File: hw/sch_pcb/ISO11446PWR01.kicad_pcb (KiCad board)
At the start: 2 copper layers, 40.1 x 40.1 mm, 17 parts, among them J1 HEADER_2x04_PARALLEL, J2 HEADER_2x04_PARALLEL, J3 HEADER_2x04_PARALLEL, J4 Conn_01x01_Female, J5 Conn_01x01_Female, J6 Conn_01x01_Female, J7 Conn_01x01_Female, J8 Umin ... Umax, M1 HOLE M3, M2 HOLE M3, M3 HOLE, M4 HOLE

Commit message: An initial test implementation. Both Schema and PCB needs check.
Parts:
- added D1: LED, Mlab_D:LED_1206, B.Cu at (169.1, 90.3)
- added D2: LED, Mlab_D:LED_1206, B.Cu at (138.6, 140.2)
- added D3: LED, Mlab_D:LED_1206, B.Cu at (129.3, 86.8)
- added D4: LED, Mlab_D:LED_1206, B.Cu at (129.2, 96.9)
- added D5: LED, Mlab_D:LED_1206, B.Cu at (129.3, 71.4)
- added D6: LED, Mlab_D:LED_1206, B.Cu at (129.3, 76.6)
- added D7: LED, Mlab_D:LED_1206, B.Cu at (129.3, 91.6)
- added D8: LED, Mlab_D:LED_1206, B.Cu at (129.2, 102.0)
- added D9: LED, Mlab_D:LED_1206, B.Cu at (129.3, 107.0)
- added F1: Polyfuse, Mlab_F:1812, B.Cu at (159.9, 132.2)
- added F4: Polyfuse, Mlab_F:1812, B.Cu at (146.5, 144.4)
- added J10: 10 - Spínané 12V +, Mlab_CON:WAGO256, F.Cu at (120.5, 116.9)
- added J11: 11 - Spínané 12V -, Mlab_CON:WAGO256, F.Cu at (120.5, 122.0)
- added J12: 12 - Not used, Mlab_CON:WAGO256, F.Cu at (120.5, 127.1)
- added J13: 13 - Trvalé 12V -, Mlab_CON:WAGO256, F.Cu at (120.5, 132.1)
- added J15: 13 - Trvalé 12V +, Mlab_CON:WAGO256, F.Cu at (178.7, 85.7)
- added J16: 13 - Trvalé 12V -, Mlab_CON:WAGO256, F.Cu at (178.7, 90.8)
- added J17: 13 - Spínané 12V +, Mlab_CON:WAGO256, F.Cu at (128.2, 144.4)
- added J18: 13 - Spínané 12V -, Mlab_CON:WAGO256, F.Cu at (128.2, 139.2)
- added J21: Signal Světel, Mlab_Pin_Headers:Straight_2x07, F.Cu at (174.2, 69.8)
- added J5: 5 - Obrsové P, Mlab_CON:WAGO256, F.Cu at (120.5, 91.5)
- added J6: 6 - Brzdové, Mlab_CON:WAGO256, F.Cu at (120.5, 96.6)
- added J7: 7 - Obrysové L, Mlab_CON:WAGO256, F.Cu at (120.5, 101.7)
- added J8: 8 - Couvací, Mlab_CON:WAGO256, F.Cu at (120.5, 106.7)
- added J9: 9 - Trvalé 12V +, Mlab_CON:WAGO256, F.Cu at (120.5, 111.8)
- added R1: 800, Mlab_R:SMD-0805, B.Cu at (169.1, 85.3)
- added R10: 240, Mlab_R:SMD-0805, B.Cu at (142.6, 104.9)
- added R11: 240, Mlab_R:SMD-0805, B.Cu at (144.4, 71.7)
- added R12: 800, Mlab_R:SMD-0805, B.Cu at (138.6, 144.3)
- added R13: 240, Mlab_R:SMD-0805, B.Cu at (152.6, 84.4)
- added R14: 240, Mlab_R:SMD-0805, B.Cu at (154.8, 105.4)
- added R15: 240, Mlab_R:SMD-0805, B.Cu at (156.3, 68.2)
- added R16: 240, Mlab_R:SMD-0805, B.Cu at (144.4, 76.2)
- added R17: 240, Mlab_R:SMD-0805, B.Cu at (140.4, 94.8)
- added R18: 240, Mlab_R:SMD-0805, B.Cu at (146.1, 115.7)
- added R19: 240, Mlab_R:SMD-0805, B.Cu at (156.6, 76.2)
- added R2: 36, Mlab_R:R_Axial_Power_L22.0mm_W9.5mm_P30.48mm, F.Cu at (134.0, 67.7)
- added R20: 240, Mlab_R:SMD-0805, B.Cu at (152.7, 94.5)
- added R21: 240, Mlab_R:SMD-0805, B.Cu at (158.3, 115.5)
- added R22: 240, Mlab_R:SMD-0805, B.Cu at (146.0, 126.3)
- added R23: 240, Mlab_R:SMD-0805, B.Cu at (158.1, 126.2)
- added R3: 36, Mlab_R:R_Axial_Power_L22.0mm_W9.5mm_P30.48mm, F.Cu at (134.0, 78.1)
- added R4: 36, Mlab_R:R_Axial_Power_L22.0mm_W9.5mm_P30.48mm, F.Cu at (134.1, 89.8)
- added R5: 36, Mlab_R:R_Axial_Power_L22.0mm_W9.5mm_P30.48mm, F.Cu at (136.7, 100.0)
- added R6: 36, Mlab_R:R_Axial_Power_L22.0mm_W9.5mm_P30.48mm, F.Cu at (140.0, 110.3)
- added R7: 36, Mlab_R:R_Axial_Power_L22.0mm_W9.5mm_P30.48mm, F.Cu at (140.1, 121.2)
- added R8: 36, Mlab_R:R_Axial_Power_L22.0mm_W9.5mm_P30.48mm, F.Cu at (140.1, 131.3)
- added R9: 240, Mlab_R:SMD-0805, B.Cu at (140.3, 84.7)
- added U1: LTV-357T, Package_SO:SO-4_4.4x3.6mm_P2.54mm, B.Cu at (146.1, 84.3)
- added U2: LTV-357T, Package_SO:SO-4_4.4x3.6mm_P2.54mm, B.Cu at (148.4, 105.4)
- added U3: LTV-357T, Package_SO:SO-4_4.4x3.6mm_P2.54mm, B.Cu at (150.0, 68.2)
- added U4: LTV-357T, Package_SO:SO-4_4.4x3.6mm_P2.54mm, B.Cu at (150.3, 76.2)
- added U5: LTV-357T, Package_SO:SO-4_4.4x3.6mm_P2.54mm, B.Cu at (146.2, 94.6)
- added U6: LTV-357T, Package_SO:SO-4_4.4x3.6mm_P2.54mm, B.Cu at (151.9, 115.5)
- added U7: LTV-357T, Package_SO:SO-4_4.4x3.6mm_P2.54mm, B.Cu at (151.8, 126.2)
- C1: footprint Capacitor_SMD:C_0805_2012Metric -> Mlab_C:SMD-0805
- F2: renamed from F1; footprint Fuse:Fuse_Bourns_MF-RG400 -> Fuse:Fuseholder_Keystone_3555-2
- F3: renamed from F2; footprint Fuse:Fuse_Bourns_MF-RG400 -> Mlab_F:1812; moved to B.Cu
- J1: renamed from J4; value Conn_01x01_Female -> 1 - Směrové L
- J14: renamed from J3; value HEADER_2x04_PARALLEL -> Trvalé 12V
- J19: renamed from J1; value HEADER_2x04_PARALLEL -> Ventilator 12V
- J2: renamed from J5; value Conn_01x01_Female -> 2 - Zadní mlhové
- J20: renamed from J2; value HEADER_2x04_PARALLEL -> Spinane 12V
- J22: renamed from J8; value Umin ... Umax -> Umin ... 5V
- J3: renamed from J6; value Conn_01x01_Female -> 3 - Kostra světla
- J4: renamed from J7; value Conn_01x01_Female -> 4 - Směrové P
- moved J20 121.1 mm to (147.5, 139.7), turned to -90 degrees
- moved J19 118.2 mm to (160.5, 139.7), turned to -90 degrees
- moved J2 110.0 mm to (120.5, 76.3), turned to 180 degrees
- moved J1 104.7 mm to (120.5, 71.2), turned to 180 degrees
- moved J3 102.7 mm to (120.5, 81.3), turned to 180 degrees
- moved J4 100.9 mm to (120.5, 86.4), turned to 180 degrees
- moved J14 98.7 mm to (173.4, 139.8), turned to 90 degrees
- moved M2 74.1 mm to (183.8, 64.1)
- moved F3 73.8 mm to (159.5, 144.5)
- moved M4 53.5 mm to (183.8, 145.4)
- moved F2 50.7 mm to (176.7, 129.4), turned to 90 degrees
- moved J22 36.8 mm to (124.1, 64.5), turned to -90 degrees
- moved C1 34.9 mm to (140.6, 72.1), turned to 0 degrees
- moved M1 34.2 mm to (112.7, 64.1)
- moved M3 33.6 mm to (112.7, 145.4)
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- renumbered D1 to D10
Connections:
- F2 pad 1: Net-(F1-Pad1) -> U12+
- F2 pad 2: Net-(F1-Pad2) -> Net-(F2-Pad2)
- F3 pad 1: Net-(F2-Pad1) -> S12+
- F3 pad 2: Net-(F2-Pad2) -> Net-(F3-Pad2)
- J1 pad 1: Net-(F1-Pad2) -> L1
- J14 pad 1: unconnected-(J3-Pad1) -> U12-
- J14 pad 2: unconnected-(J3-Pad1) -> U12-
- J14 pad 3: unconnected-(J3-Pad3) -> Net-(F1-Pad2)
- J14 pad 4: unconnected-(J3-Pad3) -> Net-(F1-Pad2)
- J14 pad 5: unconnected-(J3-Pad5) -> Net-(F1-Pad2)
- J14 pad 6: unconnected-(J3-Pad5) -> Net-(F1-Pad2)
- J14 pad 7: Net-(J1-Pad1) -> U12-
- J14 pad 8: Net-(J1-Pad1) -> U12-
- J19 pad 1: Net-(J1-Pad1) -> S12-
- J19 pad 2: Net-(J1-Pad1) -> S12-
- J19 pad 3: Net-(J1-Pad3) -> Net-(F3-Pad2)
- J19 pad 4: Net-(J1-Pad3) -> Net-(F3-Pad2)
- J19 pad 5: Net-(F2-Pad1) -> Net-(F3-Pad2)
- J19 pad 6: Net-(F2-Pad1) -> Net-(F3-Pad2)
- J19 pad 7: Net-(F1-Pad1) -> S12-
- J19 pad 8: Net-(F1-Pad1) -> S12-
- J2 pad 1: Net-(F2-Pad2) -> L2
- J20 pad 1: unconnected-(J2-Pad1) -> S12-
- J20 pad 2: unconnected-(J2-Pad1) -> S12-
- J20 pad 3: unconnected-(J2-Pad3) -> Net-(F4-Pad2)
- J20 pad 4: unconnected-(J2-Pad3) -> Net-(F4-Pad2)
- J20 pad 5: Net-(F1-Pad1) -> Net-(F4-Pad2)
- J20 pad 6: Net-(F1-Pad1) -> Net-(F4-Pad2)
- J20 pad 7: Net-(F1-Pad1) -> S12-
- J20 pad 8: Net-(F1-Pad1) -> S12-
- J3 pad 1: Net-(J1-Pad3) -> L_GND
- J4 pad 1: Net-(J1-Pad1) -> L4
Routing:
- net Net-(M1-Pad1): track 0.00 -> 235.8 mm
- net L_GND: track 0.00 -> 166.0 mm
- net +5V: track 0.00 -> 155.1 mm
- net GND: track 0.00 -> 143.4 mm
- net U12-: track 0.00 -> 135.0 mm
- net U12+: track 0.00 -> 92.7 mm
- net L8S: track 0.00 -> 90.2 mm
- net S12-: track 0.00 -> 89.9 mm
- net S12+: track 0.00 -> 83.6 mm
- net L7S: track 0.00 -> 78.2 mm
- net L6S: track 0.00 -> 68.3 mm
- net L5S: track 0.00 -> 57.1 mm
- net Net-(F2-Pad2): track 0.00 -> 45.8 mm
- net L4S: track 0.00 -> 45.2 mm
- net L8: track 0.00 -> 40.4 mm
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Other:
- board size 40.1 x 40.1 mm -> 80.8 x 90.9 mm

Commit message: slove some warnings.
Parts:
- moved D1 0.61 mm to (168.5, 90.1)
- moved J15 0.61 mm to (178.1, 85.5)
- moved J16 0.61 mm to (178.1, 90.6)
- moved R1 0.61 mm to (168.5, 85.1)
- moved D4 0.40 mm to (129.6, 96.7)
- moved D8 0.38 mm to (129.6, 102.0)
- moved D7 0.24 mm to (129.6, 91.5)
- moved D3 0.24 mm to (129.6, 86.7)
- moved D5 0.24 mm to (129.6, 71.5)
- moved D6 0.24 mm to (129.6, 76.6)
- moved R12 0.19 mm to (138.6, 144.5)
- moved D9 0.13 mm to (129.4, 107.0)
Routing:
- net L_GND: track 166.0 -> 208.7 mm
- net Net-(M1-Pad1): track 235.8 -> 230.8 mm
- net Net-(U6-Pad1): track 0.00 -> 2.72 mm
- net GND: track 143.4 -> 140.9 mm
- net S12-: track 89.9 -> 88.2 mm
- net L1: track 20.2 -> 18.6 mm
- net Net-(F1-Pad2): track 22.3 -> 21.4 mm
- net Net-(F4-Pad2): track 12.0 -> 11.2 mm
- net +5V: track 155.1 -> 154.5 mm
- net U12-: track 135.0 -> 134.4 mm
- net Net-(F2-Pad2): track 45.8 -> 46.4 mm

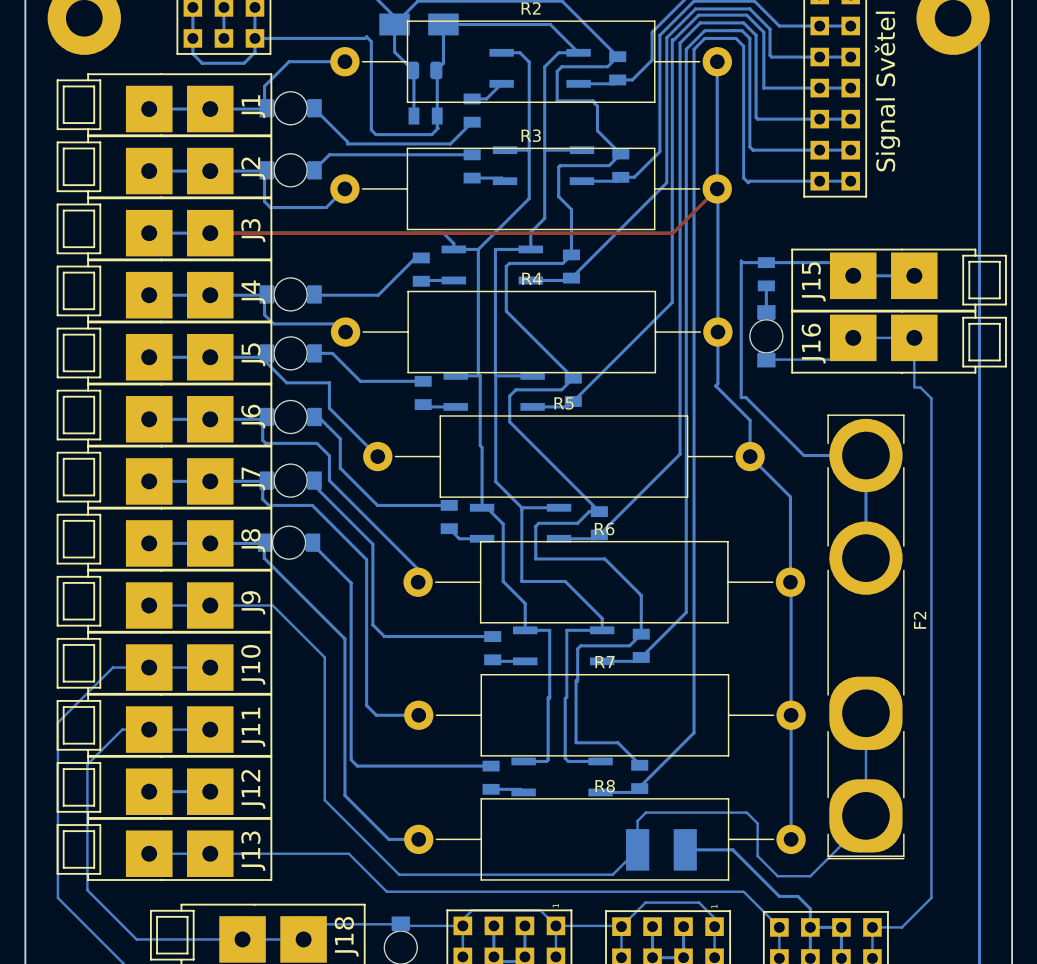
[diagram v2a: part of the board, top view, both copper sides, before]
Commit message: Improve layout and connector orientation.
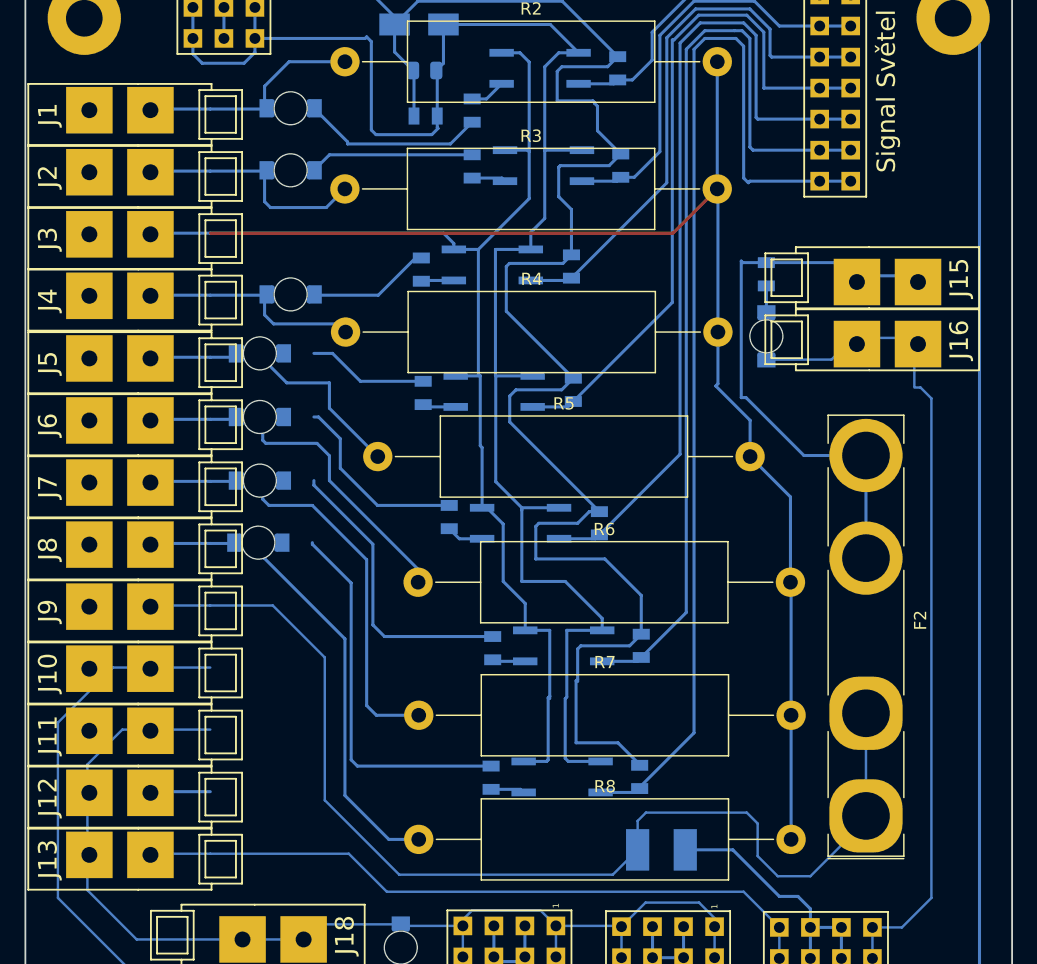
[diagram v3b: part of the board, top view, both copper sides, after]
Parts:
- moved J1 5.04 mm to (115.6, 72.0), turned to 0 degrees
- moved J10 5.04 mm to (115.6, 117.7), turned to 0 degrees
- moved J11 5.04 mm to (115.6, 122.8), turned to 0 degrees
- moved J12 5.04 mm to (115.6, 127.9), turned to 0 degrees
- moved J13 5.04 mm to (115.6, 132.9), turned to 0 degrees
- moved J2 5.04 mm to (115.6, 77.1), turned to 0 degrees
- moved J3 5.04 mm to (115.6, 82.1), turned to 0 degrees
- moved J5 5.04 mm to (115.6, 92.3), turned to 0 degrees
- moved J6 5.04 mm to (115.6, 97.4), turned to 0 degrees
- moved J7 5.04 mm to (115.6, 102.5), turned to 0 degrees
- moved J8 5.04 mm to (115.6, 107.5), turned to 0 degrees
- moved J9 5.04 mm to (115.6, 112.6), turned to 0 degrees
- moved J4 5.03 mm to (115.6, 87.2), turned to 0 degrees
- moved D4 2.52 mm to (127.1, 96.7)
- moved D7 2.52 mm to (127.1, 91.5)
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
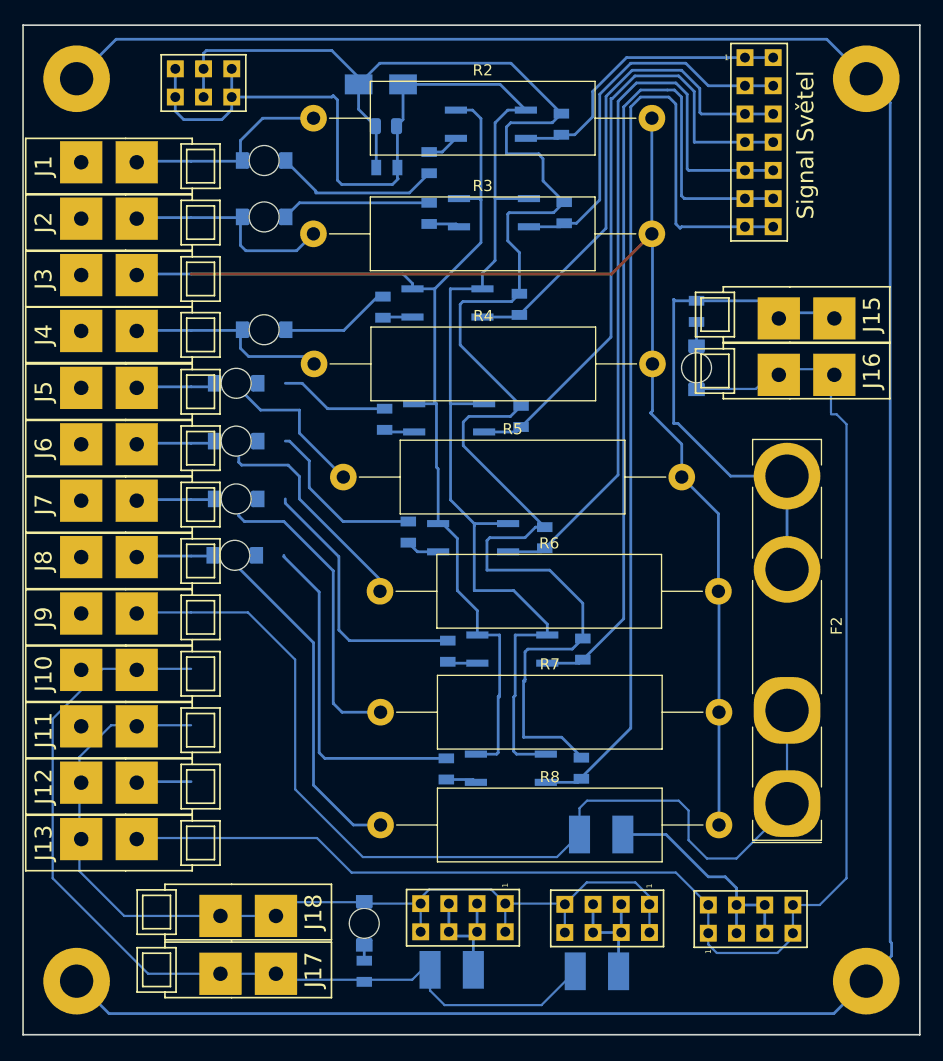
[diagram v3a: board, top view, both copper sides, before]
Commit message: Significant schematic and layout improvement. Fixed fuse footprint Fixed schematics   * Spliting to multiple sheets   * Texts translated from czech to english
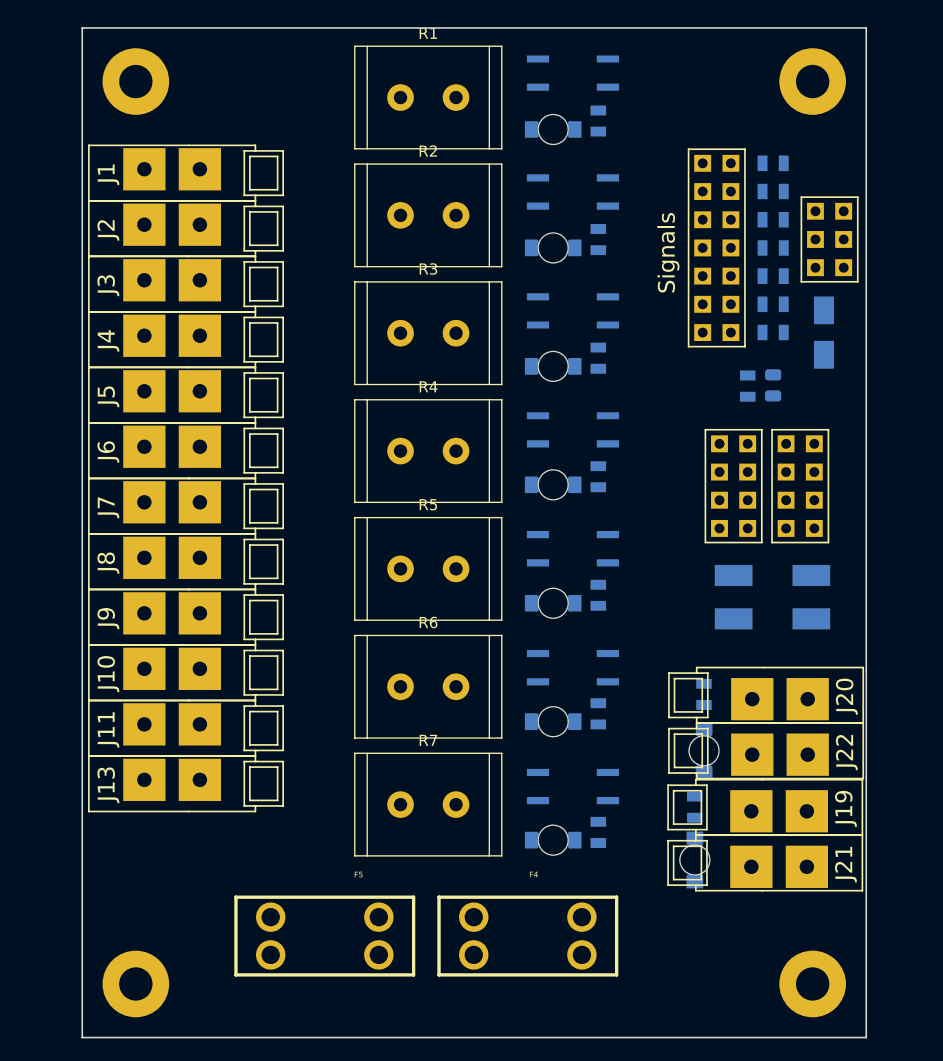
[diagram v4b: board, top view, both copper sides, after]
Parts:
- removed F2: Fuse, Fuse:Fuseholder_Keystone_3555-2
- removed J12: 12 - Not used, Mlab_CON:WAGO256
- removed J17: 13 - Spínané 12V +, Mlab_CON:WAGO256
- added F5: 16A, Mlab_CON:Fuse-Keystone-3557-2, F.Cu at (135.0, 141.3)
- D1: value LED -> BZV55C-5,6V; footprint Mlab_D:LED_1206 -> Diode_SMD:D_SMA
- D10: value BZV55C-5,6V -> LED; footprint Diode_SMD:D_SMA -> Mlab_D:LED_1206
- F1, F3: value Polyfuse -> SD110-16
- F4: value Polyfuse -> 16A; footprint Mlab_F:1812 -> Mlab_CON:Fuse-Keystone-3557-2; moved to F.Cu
- J1: value 1 - Směrové L -> WAGO 256-401
- J10: value 10 - Spínané 12V + -> WAGO 256-401
- J11: value 11 - Spínané 12V - -> WAGO 256-401
- J13: value 13 - Trvalé 12V - -> WAGO 256-401
- J14: value Trvalé 12V -> 3.3-5V; footprint Mlab_Pin_Headers:Straight_2x04 -> Mlab_Pin_Headers:Straight_2x03
- J15: value 13 - Trvalé 12V + -> Signals; footprint Mlab_CON:WAGO256 -> Mlab_Pin_Headers:Straight_2x07
- J16: value 13 - Trvalé 12V - -> 2x4; footprint Mlab_CON:WAGO256 -> Mlab_Pin_Headers:Straight_2x04
- J18: value 13 - Spínané 12V - -> 2x4; footprint Mlab_CON:WAGO256 -> Mlab_Pin_Headers:Straight_2x04
- J19: value Ventilator 12V -> WAGO 256-401; footprint Mlab_Pin_Headers:Straight_2x04 -> Mlab_CON:WAGO256
- J2: value 2 - Zadní mlhové -> WAGO 256-401
- J20: value Spinane 12V -> WAGO 256-401; footprint Mlab_Pin_Headers:Straight_2x04 -> Mlab_CON:WAGO256
- J21: value Signal Světel -> WAGO 256-401; footprint Mlab_Pin_Headers:Straight_2x07 -> Mlab_CON:WAGO256
- J22: value Umin ... 5V -> WAGO 256-401; footprint Mlab_Pin_Headers:Straight_2x03 -> Mlab_CON:WAGO256
- J3: value 3 - Kostra světla -> WAGO 256-401
- J4: value 4 - Směrové P -> WAGO 256-401
- J5: value 5 - Obrsové P -> WAGO 256-401
- J6: value 6 - Brzdové -> WAGO 256-401
- J7: value 7 - Obrysové L -> WAGO 256-401
- J8: value 8 - Couvací -> WAGO 256-401
- J9: value 9 - Trvalé 12V + -> WAGO 256-401
- R1: value 800 -> 33R; footprint Mlab_R:SMD-0805 -> Resistor_THT:R_Radial_Power_L13.0mm_W9.0mm_P5.00mm; moved to F.Cu
- R10, R11, R14, R15, R19, R20, R21: value 240 -> 510R
- R12: value 800 -> 1k
- R13, R16, R17, R18, R22, R23, R9: value 240 -> 1k
- R2, R3, R4, R5, R6, R7: value 36 -> 33R; footprint Mlab_R:R_Axial_Power_L22.0mm_W9.5mm_P30.48mm -> Resistor_THT:R_Radial_Power_L13.0mm_W9.0mm_P5.00mm
- R8: value 36 -> 1k; footprint Mlab_R:R_Axial_Power_L22.0mm_W9.5mm_P30.48mm -> Mlab_R:SMD-0805; moved to B.Cu
- moved J22 79.5 mm to (176.1, 124.6), turned to 180 degrees
- moved R12 77.1 mm to (175.4, 76.8), turned to 180 degrees
- moved D2 73.5 mm to (155.6, 68.7), turned to 0 degrees
- moved R8 69.3 mm to (175.4, 71.7), turned to 180 degrees
- moved D10 66.7 mm to (169.2, 124.6), turned to -90 degrees
- moved J21 64.9 mm to (176.0, 134.7), turned to 180 degrees
- moved J14 61.6 mm to (180.5, 78.6), turned to 180 degrees
- moved J18 58.1 mm to (171.9, 100.8), turned to 0 degrees
- moved D9 49.7 mm to (168.4, 134.5), turned to -90 degrees
- moved D6 43.5 mm to (155.6, 111.3)
- moved C2 42.0 mm to (175.4, 91.7), turned to -90 degrees
- moved D8 42.0 mm to (155.6, 132.7)
- moved D7 41.8 mm to (155.6, 122.0)
- moved R18 41.0 mm to (175.4, 87.0), turned to 180 degrees
- moved R10 40.8 mm to (159.7, 67.9), turned to 90 degrees
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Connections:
- D1 pad 1: U12- -> +5V
- D1 pad 2: Net-(D1-Pad2) -> GND
- D10 pad 1: +5V -> GND_Switched
- D10 pad 2: GND -> Net-(D10-Pad2)
- D2 pad 1: S12- -> Net-(D2-Pad1)
- D2 pad 2: Net-(D2-Pad2) -> Left_Turn_Signal_Lamp
- D3 pad 2: L4 -> Rear_Fog_Lamps
- D4 pad 2: L6 -> Right_Turn_Signal_Lamp
- D5 pad 2: L1 -> Tail_Lamps_Right
- D6 pad 2: L2 -> Stop_Lamps
- D7 pad 2: L5 -> Tail_Lamps_Left
- D8 pad 2: L7 -> Reversing_Lamps
- D9 pad 1: Net-(D9-Pad1) -> GND_Permanent
- D9 pad 2: L8 -> Net-(D9-Pad2)
- F1 pad 1: U12+ -> Net-(F1-Pad1)
- F3 pad 1: S12+ -> Net-(F3-Pad1)
- F4 pad 1: S12+ -> Net-(F1-Pad1)
- F4 pad 2: Net-(F4-Pad2) -> 12V_Switched
- J1 pad 1: L1 -> Left_Turn_Signal_Lamp
- J10 pad 1: S12+ -> 12V_Switched
- J11 pad 1: S12- -> GND_Switched
- J13 pad 1: U12- -> GND_Permanent
- J14 pad 1: U12- -> GND
- J14 pad 2: U12- -> GND
- J14 pad 3: Net-(F1-Pad2) -> +5V
- J14 pad 4: Net-(F1-Pad2) -> +5V
- J14 pad 5: Net-(F1-Pad2) -> GND
- J14 pad 6: Net-(F1-Pad2) -> GND
- J15 pad 1: Net-(F2-Pad2) -> Left_Turn_Signal
- J16 pad 1: U12- -> GND_Switched
- J18 pad 1: S12- -> GND_Permanent
- J19 pad 1: S12- -> Net-(F3-Pad1)
- J2 pad 1: L2 -> Rear_Fog_Lamps
- J20 pad 1: S12- -> Net-(F1-Pad1)
- J21 pad 1: L1S -> GND_Permanent
- J22 pad 1: GND -> GND_Switched
- J3 pad 1: L_GND -> Earth
- J4 pad 1: L4 -> Right_Turn_Signal_Lamp
- J5 pad 1: L5 -> Tail_Lamps_Right
- J6 pad 1: L6 -> Stop_Lamps
- J7 pad 1: L7 -> Tail_Lamps_Left
- J8 pad 1: L8 -> Reversing_Lamps
- J9 pad 1: U12+ -> 12V_Permanent
- M1 pad 1: Net-(M1-Pad1) -> unconnected-(M1-Pad1)
- M2 pad 1: Net-(M1-Pad1) -> unconnected-(M2-Pad1)
- M3 pad 1: Net-(M1-Pad1) -> unconnected-(M3-Pad1)
- M4 pad 1: Net-(M1-Pad1) -> unconnected-(M4-Pad1)
- R1 pad 1: Net-(F2-Pad2) -> Left_Turn_Signal_Lamp
- R1 pad 2: Net-(D1-Pad2) -> Earth
- R10 pad 1: Net-(D4-Pad1) -> Net-(D2-Pad1)
- R10 pad 2: Net-(U2-Pad1) -> Net-(R10-Pad2)
- R11 pad 1: Net-(D5-Pad1) -> Net-(D3-Pad1)
- R11 pad 2: Net-(U3-Pad1) -> Net-(R11-Pad2)
- R12 pad 1: S12+ -> +5V
- R12 pad 2: Net-(D2-Pad2) -> Right_Turn_Signal
- R13 pad 2: L4S -> Tail_Lamps_Right_Signal
- R14 pad 1: +5V -> Net-(D4-Pad1)
- R14 pad 2: L6S -> Net-(R14-Pad2)
- R15 pad 1: +5V -> Net-(D5-Pad1)
- R15 pad 2: L1S -> Net-(R15-Pad2)
- R16 pad 1: Net-(D6-Pad1) -> +5V
- R16 pad 2: Net-(R16-Pad2) -> Stop_Signal
- R17 pad 1: Net-(D7-Pad1) -> +5V
- R17 pad 2: Net-(R17-Pad2) -> Tail_Lamps_Left_Signal
- R18 pad 1: Net-(D8-Pad1) -> +5V
- R18 pad 2: Net-(U6-Pad1) -> Reversing_Signal
- R19 pad 1: +5V -> Net-(D6-Pad1)
- R19 pad 2: L2S -> Net-(R19-Pad2)
- R2 pad 1: L1 -> Rear_Fog_Lamps
- R2 pad 2: L_GND -> Earth
- R20 pad 1: +5V -> Net-(D7-Pad1)
- R20 pad 2: L5S -> Net-(R20-Pad2)
- R21 pad 1: +5V -> Net-(D8-Pad1)
- R21 pad 2: L7S -> Net-(R21-Pad2)
- R22 pad 1: Net-(D9-Pad1) -> Net-(F3-Pad1)
- R22 pad 2: Net-(U7-Pad1) -> Net-(D9-Pad2)
- R23 pad 1: +5V -> Net-(F1-Pad1)
- R23 pad 2: L8S -> Net-(D10-Pad2)
- R3 pad 1: L2 -> Right_Turn_Signal_Lamp
- R3 pad 2: L_GND -> Earth
- R4 pad 1: L4 -> Tail_Lamps_Right
- R4 pad 2: L_GND -> Earth
- R5 pad 1: L5 -> Stop_Lamps
- R5 pad 2: L_GND -> Earth
- R6 pad 1: L6 -> Tail_Lamps_Left
- R6 pad 2: L_GND -> Earth
- R7 pad 1: L7 -> Reversing_Lamps
- R7 pad 2: L_GND -> Earth
- R8 pad 1: L8 -> +5V
- R8 pad 2: L_GND -> Left_Turn_Signal
- R9 pad 1: Net-(D3-Pad1) -> +5V
- R9 pad 2: Net-(U1-Pad1) -> Rear_Fog_Signal
- U1 pad 1: Net-(U1-Pad1) -> Net-(R10-Pad2)
- U1 pad 2: L_GND -> Earth
- U1 pad 4: L4S -> Left_Turn_Signal
- U2 pad 1: Net-(U2-Pad1) -> Net-(R11-Pad2)
- U2 pad 2: L_GND -> Earth
- U2 pad 4: L6S -> Rear_Fog_Signal
- U3 pad 1: Net-(U3-Pad1) -> Net-(R14-Pad2)
- U3 pad 2: L_GND -> Earth
- U3 pad 4: L1S -> Right_Turn_Signal
- U4 pad 1: Net-(R16-Pad2) -> Net-(R15-Pad2)
- U4 pad 2: L_GND -> Earth
- U4 pad 4: L2S -> Tail_Lamps_Right_Signal
- U5 pad 1: Net-(R17-Pad2) -> Net-(R19-Pad2)
- U5 pad 2: L_GND -> Earth
- U5 pad 4: L5S -> Stop_Signal
- U6 pad 1: Net-(U6-Pad1) -> Net-(R20-Pad2)
- U6 pad 2: L_GND -> Earth
- U6 pad 4: L7S -> Tail_Lamps_Left_Signal
- U7 pad 1: Net-(U7-Pad1) -> Net-(R21-Pad2)
- U7 pad 2: L_GND -> Earth
- U7 pad 4: L8S -> Reversing_Signal
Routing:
- net Net-(M1-Pad1): track 230.8 -> 0.00 mm
- net L_GND: track 208.7 -> 0.00 mm
- net +5V: track 154.5 -> 0.00 mm
- net GND: track 140.9 -> 0.00 mm
- net U12-: track 134.4 -> 0.00 mm
- net U12+: track 92.5 -> 0.00 mm
- net L8S: track 90.2 -> 0.00 mm
- net S12-: track 88.2 -> 0.00 mm
- net S12+: track 83.6 -> 0.00 mm
- net L7S: track 78.0 -> 0.00 mm
- net L6S: track 68.3 -> 0.00 mm
- net L5S: track 57.1 -> 0.00 mm
- net Net-(F2-Pad2): track 46.4 -> 0.00 mm
- net L4S: track 45.2 -> 0.00 mm
- net L8: track 40.4 -> 0.00 mm
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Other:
- board size 80.8 x 90.9 mm -> 70.6 x 90.9 mm
